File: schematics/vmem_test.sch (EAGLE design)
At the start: 10 parts, among them IC1 ATMEGA644A, IC2 M68AW128MND, IC3 74ALS746N

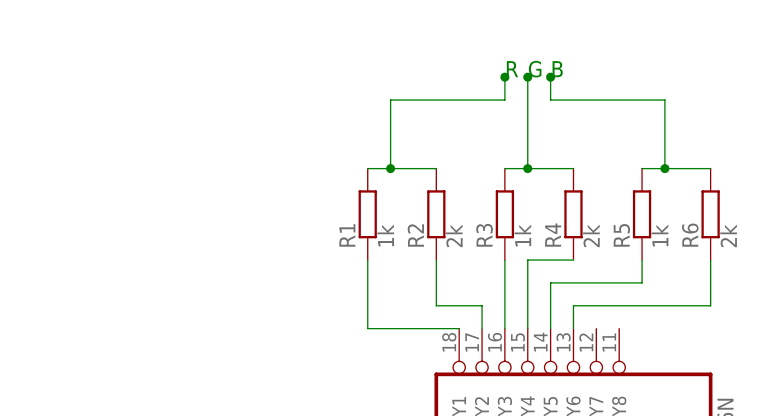
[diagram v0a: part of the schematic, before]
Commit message: Added updated schematic with new MCU and video memory
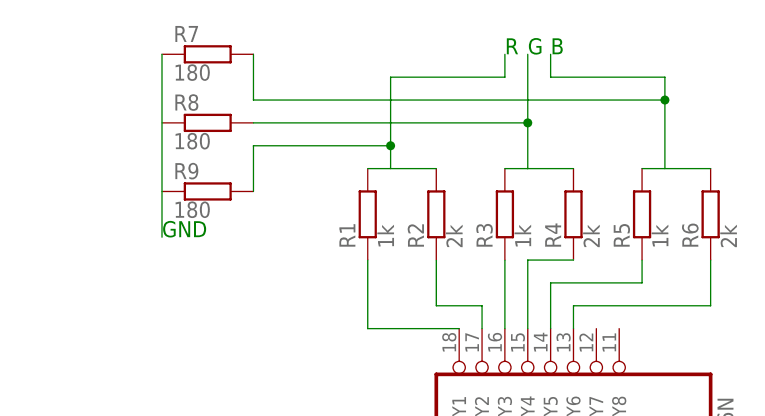
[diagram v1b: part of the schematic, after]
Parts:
- added R7, R8, R9: 180, resistor-shunt:BVS
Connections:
- new net N$33: R7.1
- new net N$35: R9.1
- new net N$38: R7.2
- net N$34: now also R8.1
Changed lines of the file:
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@@
 <part name="R5" library="resistor-shunt" deviceset="BVS" device="" value="1k"/>
 <part name="R6" library="resistor-shunt" deviceset="BVS" device="" value="2k"/>
+<part name="R7" library="resistor-shunt" deviceset="BVS" device="" value="180"/>
+<part name="R8" library="resistor-shunt" deviceset="BVS" device="" value="180"/>
+<part name="R9" library="resistor-shunt" deviceset="BVS" device="" value="180"/>
 </parts>
 <sheets>
@@
 <text x="-71.12" y="106.68" size="1.778" layer="91">Vcc</text>
 <text x="-71.12" y="35.56" size="1.778" layer="91">GND</text>
-<text x="81.28" y="172.72" size="1.778" layer="91">R</text>
-<text x="83.82" y="172.72" size="1.778" layer="91">G</text>
-<text x="86.36" y="172.72" size="1.778" layer="91">B</text>
+<text x="81.28" y="175.26" size="1.778" layer="91">R</text>
+<text x="83.82" y="175.26" size="1.778" layer="91">G</text>
+<text x="86.36" y="175.26" size="1.778" layer="91">B</text>
 <text x="7.62" y="60.96" size="1.778" layer="91">HSYNC</text>
 <text x="7.62" y="63.5" size="1.778" layer="91">VSYNC</text>
@@
 <text x="101.6" y="55.88" size="1.778" layer="91">GND</text>
 <text x="7.62" y="66.04" size="1.778" layer="91">Write</text>
+<text x="43.18" y="154.94" size="1.778" layer="91">GND</text>
 </plain>
 <instances>
@@
 <instance part="R5" gate="G$1" x="96.52" y="157.48" rot="R90"/>
 <instance part="R6" gate="G$1" x="104.14" y="157.48" rot="R90"/>
+<instance part="R7" gate="G$1" x="48.26" y="175.26"/>
+<instance part="R8" gate="G$1" x="48.26" y="167.64"/>
+<instance part="R9" gate="G$1" x="48.26" y="160.02"/>
 </instances>
 <busses>
@@
 <net name="N$33" class="0">
 <segment>
+<wire x1="99.06" y1="162.56" x2="99.06" y2="170.18" width="0.1524" layer="91"/>
+<wire x1="99.06" y1="170.18" x2="99.06" y2="172.72" width="0.1524" layer="91"/>
+<wire x1="86.36" y1="175.26" x2="86.36" y2="172.72" width="0.1524" layer="91"/>
+<wire x1="86.36" y1="172.72" x2="99.06" y2="172.72" width="0.1524" layer="91"/>
+<pinref part="R7" gate="G$1" pin="1"/>
+<wire x1="53.34" y1="175.26" x2="53.34" y2="170.18" width="0.1524" layer="91"/>
+<wire x1="53.34" y1="170.18" x2="99.06" y2="170.18" width="0.1524" layer="91"/>
+<junction x="99.06" y="170.18"/>
+</segment>
+</net>
+<net name="N$34" class="0">
+<segment>
+<pinref part="R4" gate="G$1" pin="1"/>
+<wire x1="88.9" y1="162.56" x2="83.82" y2="162.56" width="0.1524" layer="91"/>
+<pinref part="R3" gate="G$1" pin="1"/>
+<wire x1="83.82" y1="162.56" x2="81.28" y2="162.56" width="0.1524" layer="91"/>
+<wire x1="83.82" y1="162.56" x2="83.82" y2="167.64" width="0.1524" layer="91"/>
+<pinref part="R8" gate="G$1" pin="1"/>
+<wire x1="83.82" y1="167.64" x2="83.82" y2="175.26" width="0.1524" layer="91"/>
+<wire x1="53.34" y1="167.64" x2="83.82" y2="167.64" width="0.1524" layer="91"/>
+<junction x="83.82" y="167.64"/>
+</segment>
+</net>
+<net name="N$35" class="0">
+<segment>
+<wire x1="68.58" y1="162.56" x2="68.58" y2="165.1" width="0.1524" layer="91"/>
+<pinref part="R9" gate="G$1" pin="1"/>
+<wire x1="68.58" y1="165.1" x2="68.58" y2="170.18" width="0.1524" layer="91"/>
+<wire x1="53.34" y1="160.02" x2="53.34" y2="165.1" width="0.1524" layer="91"/>
+<wire x1="53.34" y1="165.1" x2="68.58" y2="165.1" width="0.1524" layer="91"/>
+<junction x="68.58" y="165.1"/>
+</segment>
+</net>
+<net name="N$36" class="0">
+<segment>
+<pinref part="R1" gate="G$1" pin="1"/>
+<pinref part="R2" gate="G$1" pin="1"/>
+<wire x1="73.66" y1="162.56" x2="66.04" y2="162.56" width="0.1524" layer="91"/>
+</segment>
+</net>
+<net name="N$37" class="0">
+<segment>
+<pinref part="R6" gate="G$1" pin="1"/>
 <pinref part="R5" gate="G$1" pin="1"/>
-<pinref part="R6" gate="G$1" pin="1"/>
-<wire x1="96.52" y1="162.56" x2="99.06" y2="162.56" width="0.1524" layer="91"/>
-<wire x1="99.06" y1="162.56" x2="104.14" y2="162.56" width="0.1524" layer="91"/>
-<wire x1="99.06" y1="162.56" x2="99.06" y2="170.18" width="0.1524" layer="91"/>
-<wire x1="99.06" y1="170.18" x2="86.36" y2="170.18" width="0.1524" layer="91"/>
-<wire x1="86.36" y1="170.18" x2="86.36" y2="172.72" width="0.1524" layer="91"/>
-<junction x="99.06" y="162.56"/>
-<junction x="86.36" y="172.72"/>
-</segment>
-</net>
-<net name="N$34" class="0">
-<segment>
-<pinref part="R4" gate="G$1" pin="1"/>
-<pinref part="R3" gate="G$1" pin="1"/>
-<wire x1="88.9" y1="162.56" x2="83.82" y2="162.56" width="0.1524" layer="91"/>
-<wire x1="83.82" y1="162.56" x2="81.28" y2="162.56" width="0.1524" layer="91"/>
-<wire x1="83.82" y1="162.56" x2="83.82" y2="172.72" width="0.1524" layer="91"/>
-<junction x="83.82" y="162.56"/>
-<junction x="83.82" y="172.72"/>
-</segment>
-</net>
-<net name="N$35" class="0">
-<segment>
-<pinref part="R2" gate="G$1" pin="1"/>
-<pinref part="R1" gate="G$1" pin="1"/>
-<wire x1="73.66" y1="162.56" x2="68.58" y2="162.56" width="0.1524" layer="91"/>
-<wire x1="68.58" y1="162.56" x2="66.04" y2="162.56" width="0.1524" layer="91"/>
-<wire x1="68.58" y1="162.56" x2="68.58" y2="170.18" width="0.1524" layer="91"/>
-<wire x1="68.58" y1="170.18" x2="81.28" y2="170.18" width="0.1524" layer="91"/>
-<wire x1="81.28" y1="170.18" x2="81.28" y2="172.72" width="0.1524" layer="91"/>
-<junction x="68.58" y="162.56"/>
-<junction x="81.28" y="172.72"/>
-</segment>
-</net>
+<wire x1="96.52" y1="162.56" x2="104.14" y2="162.56" width="0.1524" layer="91"/>
+</segment>
+</net>
+<net name="N$39" class="0">
+<segment>
+<wire x1="68.58" y1="170.18" x2="68.58" y2="172.72" width="0.1524" layer="91"/>
+<wire x1="68.58" y1="172.72" x2="81.28" y2="172.72" width="0.1524" layer="91"/>
+<wire x1="81.28" y1="172.72" x2="81.28" y2="175.26" width="0.1524" layer="91"/>
+</segment>
+</net>
+<net name="N$38" class="0">
+<segment>
+<pinref part="R7" gate="G$1" pin="2"/>
+<wire x1="43.18" y1="175.26" x2="43.18" y2="154.94" width="0.1524" layer="91"/>
+</segment>
+</net>

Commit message: minor mistake ...
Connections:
- new net N$40: IC1.(PCINT12/OC0B/!SS!)PB4, IC2G$1.A16
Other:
- note added: "Bank"
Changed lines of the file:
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@@
 <text x="7.62" y="66.04" size="1.778" layer="91">Write</text>
 <text x="43.18" y="154.94" size="1.778" layer="91">GND</text>
+<text x="10.16" y="71.12" size="1.778" layer="91">Bank</text>
 </plain>
 <instances>
@@
 </segment>
 </net>
+<net name="N$40" class="0">
+<segment>
+<pinref part="IC2" gate="G$1" pin="A16"/>
+<wire x1="81.28" y1="66.04" x2="81.28" y2="60.96" width="0.1524" layer="91"/>
+<wire x1="81.28" y1="60.96" x2="20.32" y2="60.96" width="0.1524" layer="91"/>
+<wire x1="20.32" y1="60.96" x2="20.32" y2="71.12" width="0.1524" layer="91"/>
+<pinref part="IC1" gate="G$1" pin="(PCINT12/OC0B/!SS!)PB4"/>
+<wire x1="20.32" y1="71.12" x2="-5.08" y2="71.12" width="0.1524" layer="91"/>
+</segment>
+</net>
